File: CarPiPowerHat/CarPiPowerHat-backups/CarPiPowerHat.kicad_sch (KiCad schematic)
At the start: 8 parts, among them J4 Conn_02x03_Counter_Clockwise, J9 Conn_01x04

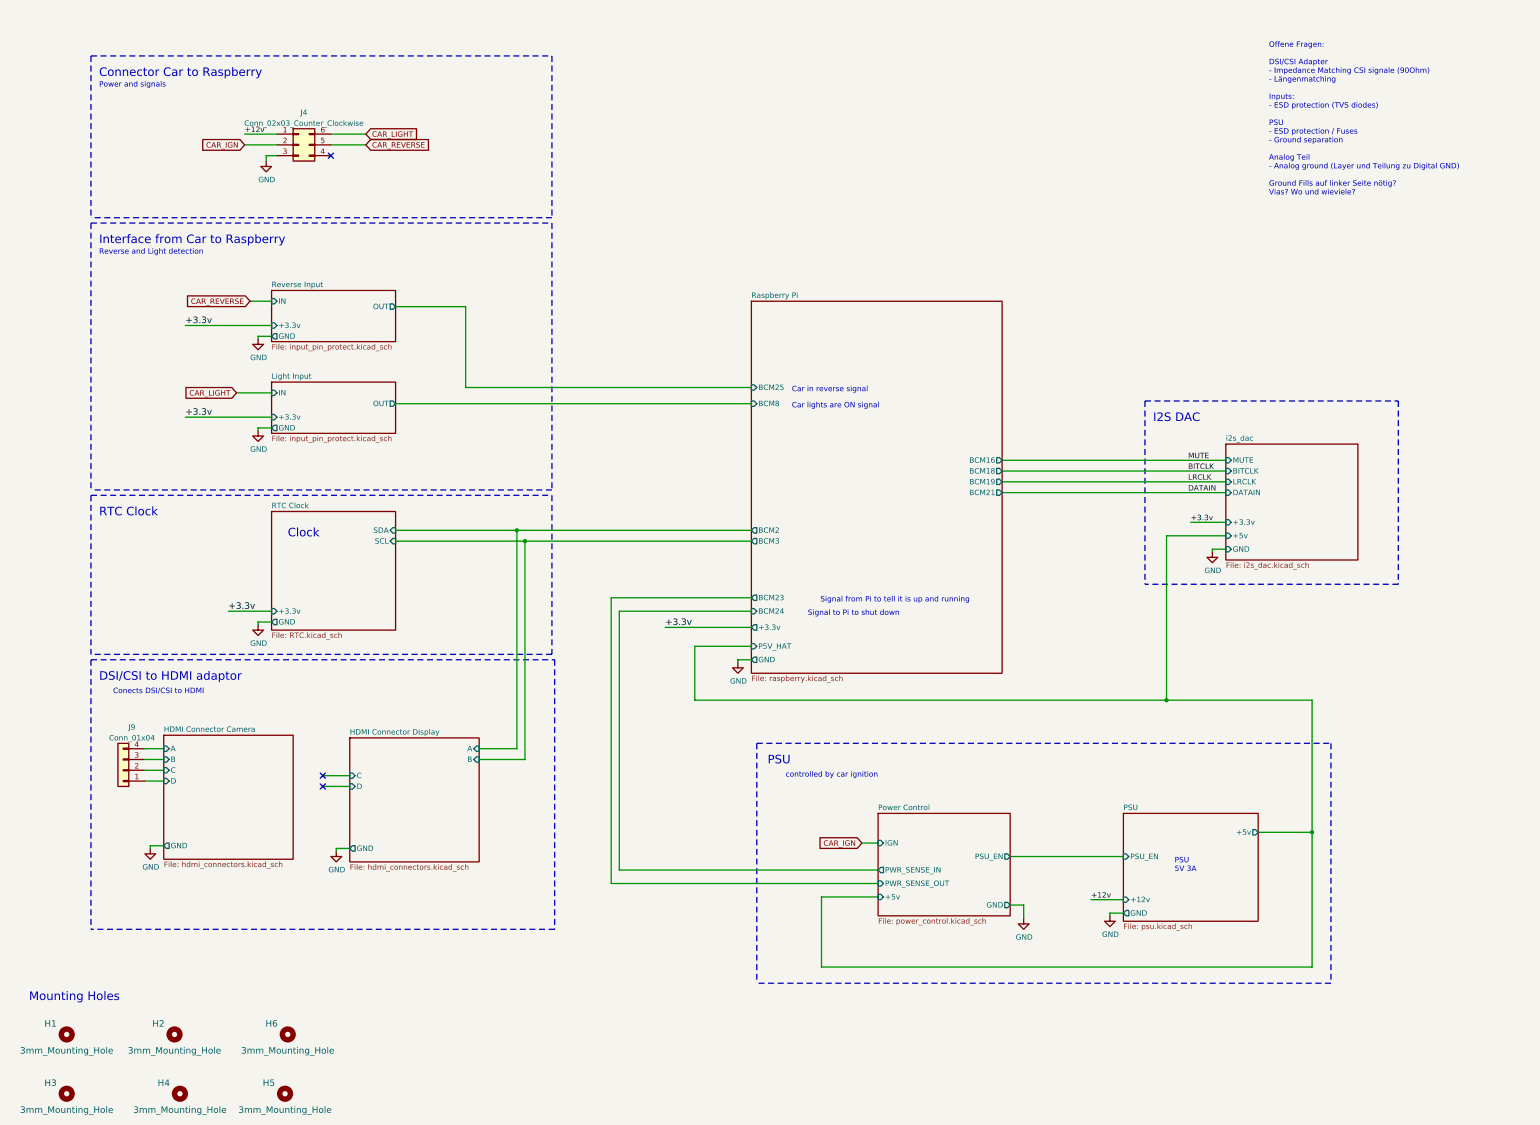
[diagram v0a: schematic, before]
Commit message: Repositioning of connectors
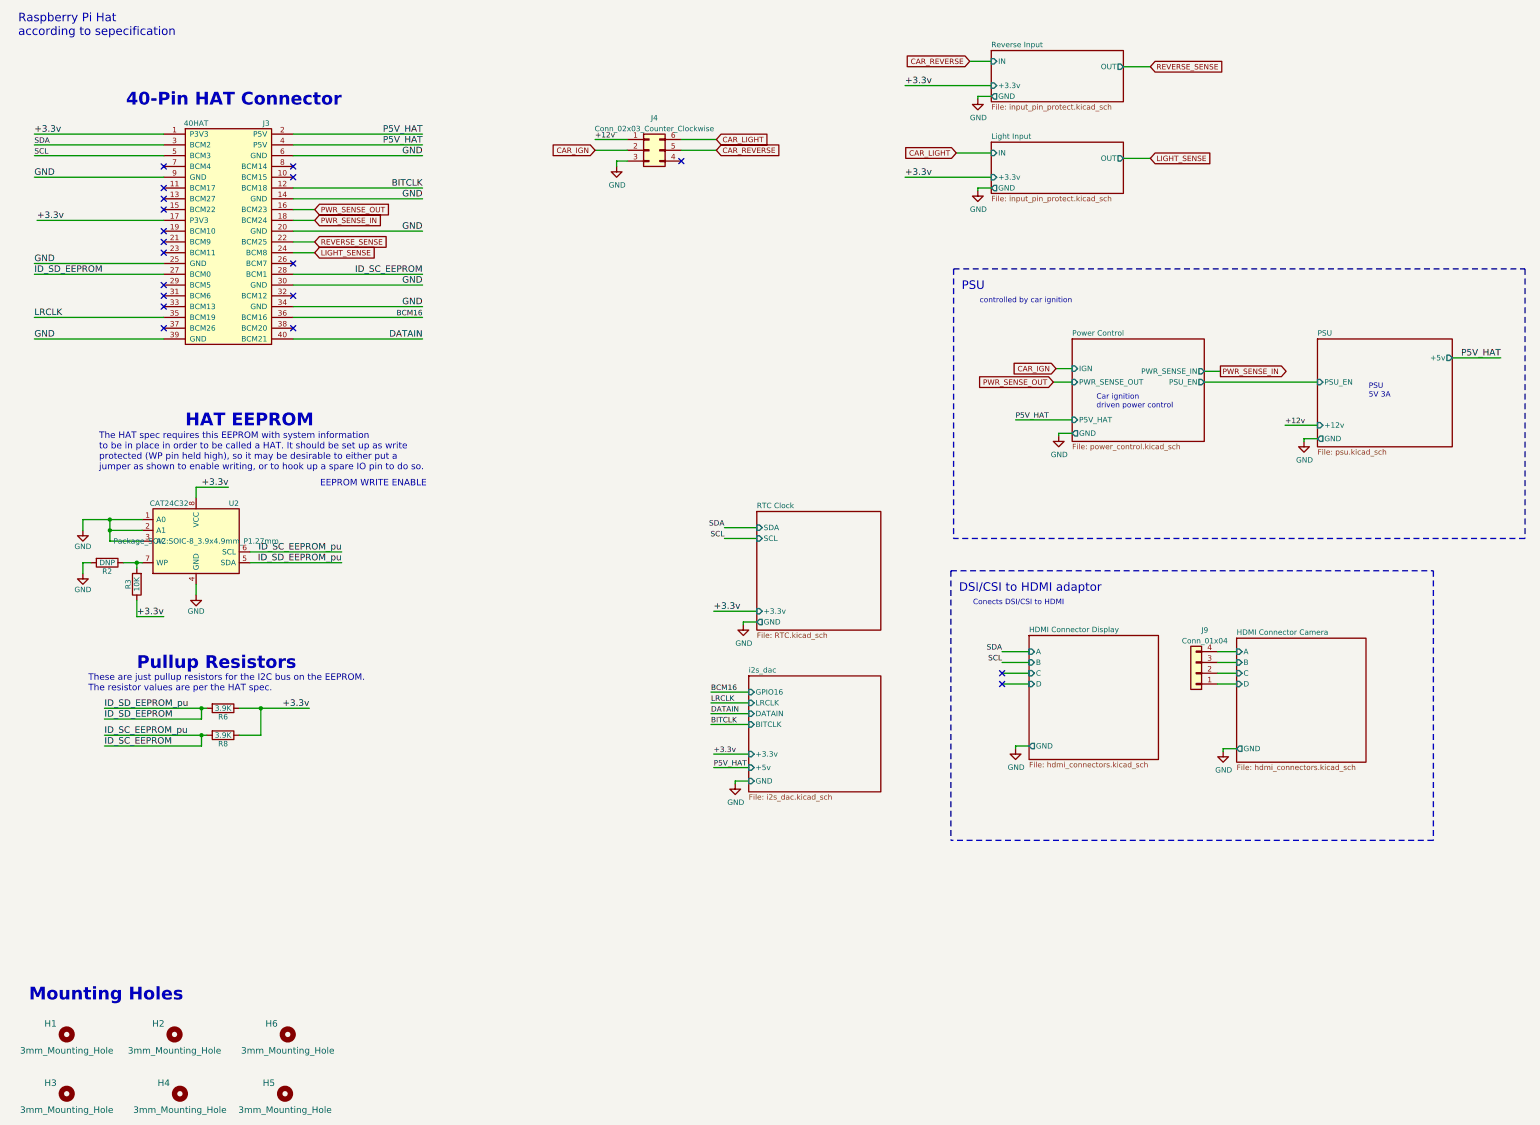
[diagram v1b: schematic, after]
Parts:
- added J3: 40HAT, Connector_PinSocket_2.54mm:PinSocket_2x20_P2.54mm_Vertical, symbol CarPiPowerHat:OX40HAT
- added R2: DNP, project_footprints:R_0603_1608Metric_Pad0.84x1.00mm_HandSolder, symbol Device:R
- added R3: 10K, Resistor_SMD:R_0603_1608Metric, symbol Device:R
- added R6, R8: 3.9K, Resistor_SMD:R_0603_1608Metric, symbol Device:R
- added U2: CAT24C32, Package_SOIC:SOIC-8_3.9x4.9mm_P1.27mm, symbol CarPiPowerHat:CAT24C32
- J4: footprint Connector_Molex:Molex_Mini-Fit_Jr_5569-06A2_2x03_P4.20mm_Horizontal -> Connector_Molex:Molex_Mini-Fit_Jr_5569-06A1_2x03_P4.20mm_Horizontal
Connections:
- net +3.3v: now also J3.1 (P3V3), J3.17 (P3V3), R3.1, R6.1, R8.1, U2.8 (VCC)
- net BITCLK: now also J3.12 (BCM18)
- net DATAIN: now also J3.40 (BCM21)
- net GND: now also J3.14 (GND), J3.20 (GND), J3.25 (GND), J3.30 (GND), J3.34 (GND), J3.39 (GND), J3.6 (GND), J3.9 (GND), R2.2, U2.1 (A0), U2.2 (A1), U2.3 (A2), U2.4 (GND)
- net LRCLK: now also J3.35 (BCM19)
- new net: R2.1, R3.2, U2.7 (WP)
- new net BCM16: J3.36 (BCM16)
- new net ID_SC_EEPROM: J3.28 (BCM1), R8.2, U2.6 (SCL)
- new net ID_SD_EEPROM: J3.27 (BCM0), R6.2, U2.5 (SDA)
- new net LIGHT_SENSE: J3.24 (BCM8)
- new net P5V_HAT: J3.2 (P5V), J3.4 (P5V)
- new net PWR_SENSE_IN: J3.18 (BCM24)
- new net PWR_SENSE_OUT: J3.16 (BCM23)
- new net REVERSE_SENSE: J3.22 (BCM25)
- new net SCL: J3.5 (BCM3)
- new net SDA: J3.3 (BCM2)
- no-connect marks 3 -> 19
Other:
- removed sheet Raspberry Pi
- sheet Power Control ports: added P5V_HAT; removed +5v
- sheet i2s_dac ports: added GPIO16; removed MUTE
- note added: "40-Pin HAT Connector"
- note added: "Car ignition driven power control"
- note added: "EEPROM WRITE ENABLE"
- note added: "HAT EEPROM"
- note added: "Pullup Resistors"
- note added: "Raspberry Pi Hat according to sepecification"
- note added: "The HAT spec requires this EEPROM with system information to be in place in order to be called a HAT. It should be set up as write protected (WP pin held high), so it may be desirable to either put a jumper as shown to enable writing, or to hook up a spare IO pin to do so."
- note added: "These are just pullup resistors for the I2C bus on the EEPROM. The resistor values are per the HAT spec."
- note removed: "Car in reverse signal"
- note removed: "Car lights are ON signal"
- note removed: "Clock"
- note removed: "Connector Car to Raspberry"
- note removed: "I2S DAC"
- note removed: "Interface from Car to Raspberry"
- note removed: "Offene Fragen: DSI/CSI Adapter - Impedance Matching CSI signale (90Ohm) - Längenmatching Inputs: - ESD protection (TVS diodes) PSU - ESD protection / Fuses - Ground separation Analog Teil - Analog ground (Layer und Teilung zu Digital GND) Ground Fills auf linker Seite nötig? Vias? Wo und wieviele?"
- note removed: "Power and signals"
- note removed: "RTC Clock"
- note removed: "Reverse and Light detection"
- note removed: "Signal from Pi to tell it is up and running"
- note removed: "Signal to Pi to shut down"
- moved on the sheet: J4, J9
